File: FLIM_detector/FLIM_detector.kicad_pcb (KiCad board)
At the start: 2 copper layers, 19.8 x 18.4 mm, 17 parts, among them J1 Conn_01x02_Female, J2 Conn_01x02_Female, U1 OPA858xDSG, U2 LM4040DBZ-2.0, U3 AMS1117-5.0

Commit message: v0.7 power connector was flipped
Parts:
- moved J1 2.60 mm to (245.0, 18.3), turned to 90 degrees
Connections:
- D2 pad 2: Net-(J1-Pad2) -> Net-(D2-Pad2)
- J1 pad 1: GND -> Net-(D2-Pad2)
- J1 pad 2: Net-(J1-Pad2) -> GND
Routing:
- net Net-(J1-Pad2): track 3.37 -> 0.00 mm
- net Net-(D2-Pad2): track 0.00 -> 3.31 mm
- net +5V: track 21.4 -> 24.4 mm
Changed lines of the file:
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@@
   (net 7 "Net-(C3-Pad2)")
   (net 8 "Net-(J2-Pad1)")
-  (net 9 "Net-(J1-Pad2)")
+  (net 9 "Net-(D2-Pad2)")
   (footprint "Resistor_SMD:R_0402_1005Metric_Pad0.72x0.64mm_HandSolder" (layer "F.Cu")
     (at 248.4 27.6 90)
@@
       (net 7 "Net-(C3-Pad2)") (pinfunction "K") (pintype "passive"))
     (pad "2" smd rect (at 1.1 0 90) (size 0.5 0.5) (layers "F.Cu" "F.Paste" "F.Mask")
-      (net 9 "Net-(J1-Pad2)") (pinfunction "A") (pintype "passive"))
+      (net 9 "Net-(D2-Pad2)") (pinfunction "A") (pintype "passive"))
     (model "${KICAD6_3DMODEL_DIR}/Diode_SMD.3dshapes/D_SOD-323F.wrl"
       (offset (xyz 0 0 0))
@@
   )
   (footprint "Connector_PinHeader_2.54mm:PinHeader_1x02_P2.54mm_Vertical" (layer "F.Cu")
-    (at 247.6 18.325 -90)
+    (at 245 18.325 90)
     (descr "Through hole straight pin header, 1x02, 2.54mm pitch, single row")
     (tags "Through hole pin header THT 1x02 2.54mm single row")
@@
     (fp_line (start -1.27 3.81) (end -1.27 -0.635) (layer "F.Fab") (width 0.1))
     (fp_line (start -1.27 -0.635) (end -0.635 -1.27) (layer "F.Fab") (width 0.1))
-    (pad "1" thru_hole rect (at 0 0 270) (size 1.7 1.7) (drill 1) (layers *.Cu *.Mask)
-      (net 3 "GND") (pinfunction "Pin_1") (pintype "passive"))
-    (pad "2" thru_hole oval (at 0 2.54 270) (size 1.7 1.7) (drill 1) (layers *.Cu *.Mask)
-      (net 9 "Net-(J1-Pad2)") (pinfunction "Pin_2") (pintype "passive"))
+    (pad "1" thru_hole rect (at 0 0 90) (size 1.7 1.7) (drill 1) (layers *.Cu *.Mask)
+      (net 9 "Net-(D2-Pad2)") (pinfunction "Pin_1") (pintype "passive"))
+    (pad "2" thru_hole oval (at 0 2.54 90) (size 1.7 1.7) (drill 1) (layers *.Cu *.Mask)
+      (net 3 "GND") (pinfunction "Pin_2") (pintype "passive"))
     (model "${KICAD6_3DMODEL_DIR}/Connector_PinHeader_2.54mm.3dshapes/PinHeader_1x02_P2.54mm_Vertical.wrl"
       (offset (xyz 0 0 0))
@@
   (via (at 252.2 21.4) (size 0.8) (drill 0.4) (layers "F.Cu" "B.Cu") (free) (net 3))
   (segment (start 245.05 23) (end 251.35 23) (width 1) (layer "F.Cu") (net 4))
-  (segment (start 251.35 23.75) (end 252.3675 24.7675) (width 0.25) (layer "F.Cu") (net 4))
+  (segment (start 251.35 23.75) (end 252.3675 24.7675) (width 0.6) (layer "F.Cu") (net 4))
   (segment (start 254.949022 29.8) (end 251.7975 29.8) (width 0.4) (layer "F.Cu") (net 4))
   (segment (start 255.6 27.2) (end 255.6 29.149022) (width 0.4) (layer "F.Cu") (net 4))
   (segment (start 252.3675 26) (end 252.3675 27.1475) (width 0.4) (layer "F.Cu") (net 4))
+  (segment (start 251.2 21.2) (end 251.2 22.85) (width 0.6) (layer "F.Cu") (net 4))
   (segment (start 251.35 23) (end 251.35 23.75) (width 0.25) (layer "F.Cu") (net 4))
-  (segment (start 252.3675 24.7675) (end 252.3675 26) (width 0.25) (layer "F.Cu") (net 4))
+  (segment (start 252.3675 24.7675) (end 252.3675 26) (width 0.6) (layer "F.Cu") (net 4))
+  (segment (start 251.2 22.85) (end 251.35 23) (width 0.6) (layer "F.Cu") (net 4))
   (segment (start 252.6 26) (end 253.509511 26.909511) (width 0.4) (layer "F.Cu") (net 4))
   (segment (start 255.309511 26.909511) (end 255.6 27.2) (width 0.4) (layer "F.Cu") (net 4))
   (segment (start 255.6 29.149022) (end 255.374511 29.374511) (width 0.4) (layer "F.Cu") (net 4))
+  (segment (start 251.2 20.0625) (end 251.2 21.2) (width 0.6) (layer "F.Cu") (net 4))
   (segment (start 252.3675 26) (end 252.6 26) (width 0.4) (layer "F.Cu") (net 4))
   (segment (start 253.509511 26.909511) (end 255.309511 26.909511) (width 0.4) (layer "F.Cu") (net 4))
@@
   (segment (start 252.41 28.19) (end 254.19 28.19) (width 0.25) (layer "F.Cu") (net 8))
   (segment (start 242.6 19.8) (end 242.6 20.1) (width 0.25) (layer "F.Cu") (net 9))
-  (segment (start 243.2 19.2) (end 242.6 19.8) (width 0.5) (layer "F.Cu") (net 9))
-  (segment (start 244.185 19.2) (end 243.2 19.2) (width 0.5) (layer "F.Cu") (net 9))
-  (segment (start 245.06 18.325) (end 244.185 19.2) (width 0.5) (layer "F.Cu") (net 9))
+  (segment (start 242.6 19.8) (end 244.075 18.325) (width 0.5) (layer "F.Cu") (net 9))
+  (segment (start 244.075 18.325) (end 245 18.325) (width 0.5) (layer "F.Cu") (net 9))
   (zone (net 3) (net_name "GND") (layers F&B.Cu) (name "GND") (hatch edge 0.508)
     (connect_pads (clearance 0.508))

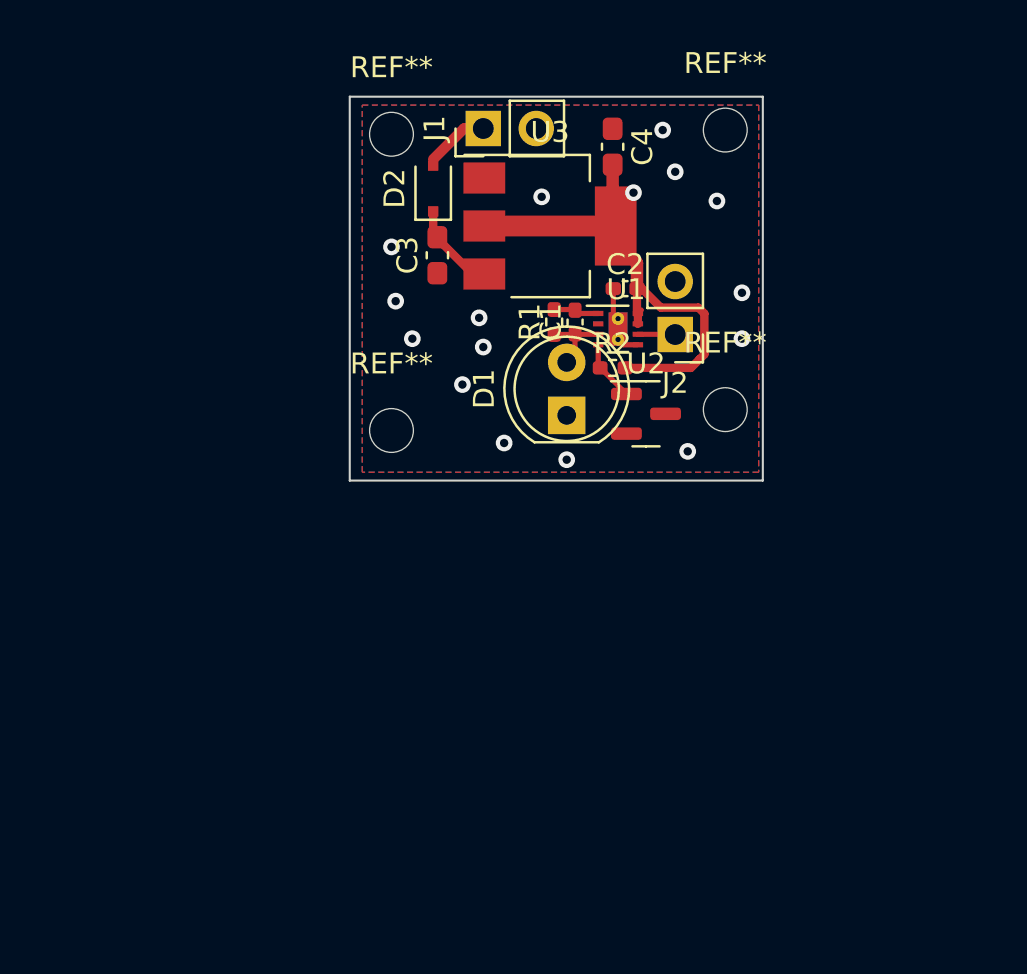
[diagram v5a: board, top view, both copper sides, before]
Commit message: v0.8 Routing was optimized
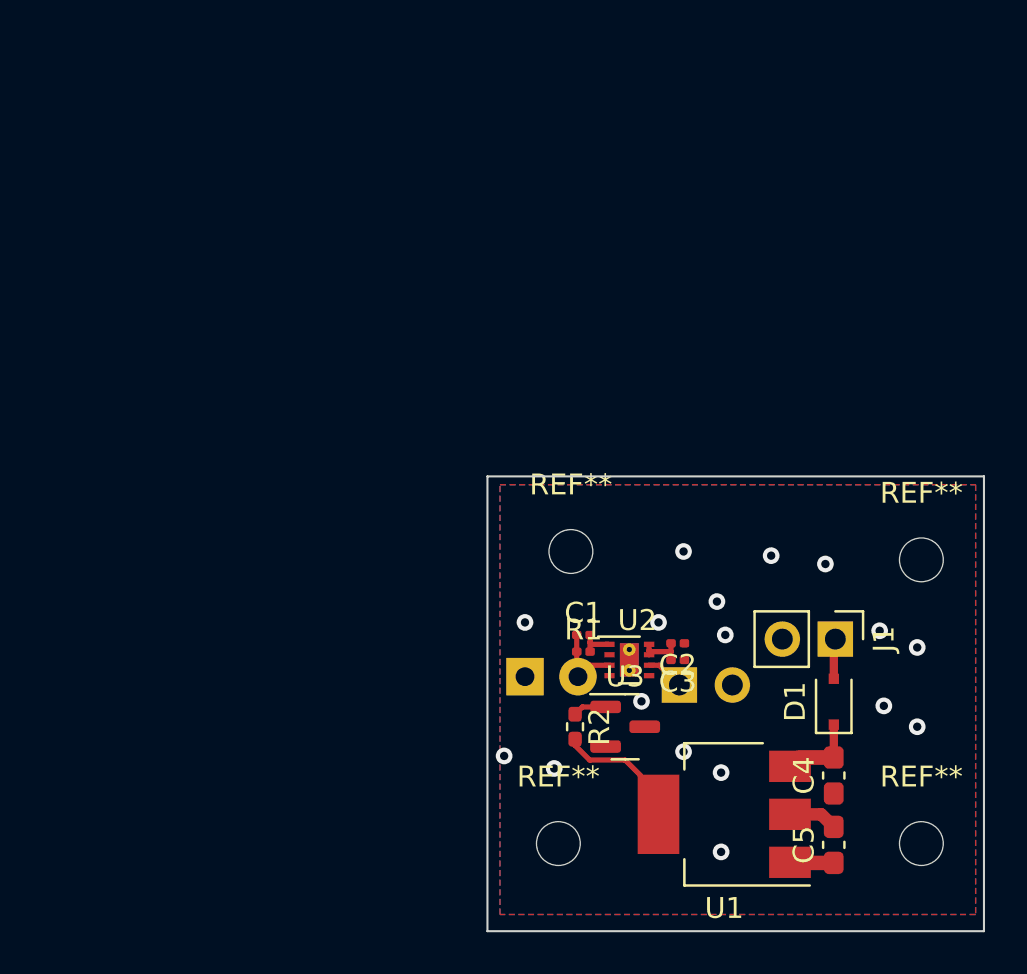
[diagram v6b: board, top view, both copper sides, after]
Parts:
- added C5: C, Capacitor_SMD:C_0603_1608Metric_Pad1.08x0.95mm_HandSolder, F.Cu at (261.8, 52.7)
- C1, C2: footprint Capacitor_SMD:C_0402_1005Metric_Pad0.74x0.62mm_HandSolder -> Capacitor_SMD:C_0201_0603Metric
- C3: footprint Capacitor_SMD:C_0603_1608Metric_Pad1.08x0.95mm_HandSolder -> Capacitor_SMD:C_0201_0603Metric
- D1: value LED -> PMEG4010CEJ; footprint LED_THT:LED_D5.0mm_Clear -> Diode_SMD:D_SOD-323F
- D2: value PMEG4010CEJ -> LED; footprint Diode_SMD:D_SOD-323F -> LED_THT:LED_D5.0mm_Clear; moved to B.Cu
- J2: moved to B.Cu
- R1: footprint Resistor_SMD:R_0402_1005Metric_Pad0.72x0.64mm_HandSolder -> Resistor_SMD:R_0201_0603Metric
- U1: value OPA858xDSG -> AMS1117-5.0; footprint Package_SON:WSON-8-1EP_2x2mm_P0.5mm_EP0.9x1.6mm_ThermalVias -> Package_TO_SOT_SMD:SOT-223-3_TabPin2
- U2: value LM4040DBZ-2.0 -> OPA858xDSG; footprint Package_TO_SOT_SMD:SOT-23 -> Package_SON:WSON-8-1EP_2x2mm_P0.5mm_EP0.9x1.6mm_ThermalVias
- U3: value AMS1117-5.0 -> LM4040DBZ-2.0; footprint Package_TO_SOT_SMD:SOT-223-3_TabPin2 -> Package_TO_SOT_SMD:SOT-23
- moved C4 31.9 mm to (261.8, 49.3), turned to 90 degrees
- moved J1 29.7 mm to (261.9, 42.8), turned to -90 degrees
- moved U3 24.3 mm to (251.8, 47.0)
- moved U1 23.8 mm to (256.6, 51.2), turned to 180 degrees
- moved D2 23.8 mm to (247.0, 44.6), turned to 0 degrees
- moved REF** 22.8 mm to (266.0, 52.6)
- moved REF** 22.6 mm to (266.0, 39.0)
- moved C3 22.6 mm to (254.3, 43.8), turned to 180 degrees
- moved REF** 21.8 mm to (249.2, 38.6)
- moved REF** 21.4 mm to (248.6, 52.6)
- moved D1 18.8 mm to (261.8, 45.8)
- moved R2 17.3 mm to (249.4, 47.0), turned to -90 degrees
- moved C2 17.2 mm to (254.3, 43.0), turned to 180 degrees
- moved J2 16.8 mm to (254.4, 45.0), turned to -90 degrees
- moved R1 15.9 mm to (249.8, 43.4), turned to 0 degrees
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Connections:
- C1 pad 1: Net-(C1-Pad1) -> Net-(U2-Pad3)
- C3 pad 2: Net-(C3-Pad2) -> +5V
- C4 pad 2: +5V -> Net-(C4-Pad2)
- D1 pad 1: GND -> Net-(C4-Pad2)
- D1 pad 2: Net-(C1-Pad1) -> Net-(D1-Pad2)
- D2 pad 1: Net-(C3-Pad2) -> GND
- D2 pad 2: Net-(D2-Pad2) -> Net-(U2-Pad3)
- J1 pad 1: Net-(D2-Pad2) -> Net-(D1-Pad2)
- R1 pad 1: Net-(C1-Pad1) -> Net-(U2-Pad3)
- U1 pad 1: Net-(C1-Pad2) -> GND
- U1 pad 2: unconnected-(U1-Pad2) -> +5V
- U1 pad 3: Net-(C1-Pad1) -> Net-(C4-Pad2)
- U2 pad 1: Net-(R2-Pad1) -> Net-(C1-Pad2)
- U2 pad 2: GND -> unconnected-(U2-Pad2)
- U2 pad 3: (no net) -> Net-(U2-Pad3)
- U3 pad 1: GND -> Net-(R2-Pad1)
- U3 pad 2: +5V -> GND
- U3 pad 3: Net-(C3-Pad2) -> (no net)
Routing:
- net +5V: track 24.4 -> 11.8 mm
- net Net-(C3-Pad2): track 4.67 -> 0.00 mm
- net Net-(C4-Pad2): track 0.00 -> 3.85 mm
- net Net-(U2-Pad3): track 0.00 -> 3.76 mm
- net Net-(C1-Pad1): track 3.70 -> 0.00 mm
- net Net-(D2-Pad2): track 3.31 -> 0.00 mm
- net Net-(D1-Pad2): track 0.00 -> 1.93 mm
- net Net-(R2-Pad1): track 2.93 -> 1.61 mm
- net (no net): vias 0 -> 1
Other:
- board size 19.8 x 18.4 mm -> 23.8 x 21.8 mm

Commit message: v0.9 subcompleted
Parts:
- moved REF** 1.28 mm to (248.2, 37.8)
- moved REF** 1.22 mm to (266.2, 37.8)
- moved REF** 1.08 mm to (248.2, 53.6)
- moved REF** 1.02 mm to (266.2, 53.6)
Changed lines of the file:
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@@
   )
   (footprint "MountingHole:MountingHole_2.1mm" (layer "F.Cu")
-    (at 249.2 38.6)
+    (at 248.2 37.8)
     (descr "Mounting Hole 2.1mm, no annular")
     (tags "mounting hole 2.1mm no annular")
@@
   )
   (footprint "MountingHole:MountingHole_2.1mm" (layer "F.Cu")
-    (at 266 52.6)
+    (at 266.2 53.6)
     (descr "Mounting Hole 2.1mm, no annular")
     (tags "mounting hole 2.1mm no annular")
@@
   )
   (footprint "MountingHole:MountingHole_2.1mm" (layer "F.Cu")
-    (at 248.6 52.6)
+    (at 248.2 53.6)
     (descr "Mounting Hole 2.1mm, no annular")
     (tags "mounting hole 2.1mm no annular")
@@
   )
   (footprint "MountingHole:MountingHole_2.1mm" (layer "F.Cu")
-    (at 266 39)
+    (at 266.2 37.8)
     (descr "Mounting Hole 2.1mm, no annular")
     (tags "mounting hole 2.1mm no annular")
@@
   (segment (start 250.8625 46.05) (end 249.7525 46.05) (width 0.25) (layer "F.Cu") (net 9))
   (zone (net 2) (net_name "GND") (layers F&B.Cu) (hatch edge 0.508)
-    (connect_pads (clearance 0.508))
-    (min_thickness 0.254) (filled_areas_thickness no)
-    (fill yes (thermal_gap 0.508) (thermal_bridge_width 0.508))
+    (connect_pads (clearance 0.2))
+    (min_thickness 0.2) (filled_areas_thickness no)
+    (fill yes (thermal_gap 0.2) (thermal_bridge_width 0.2))
     (polygon
       (pts

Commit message: v0.91 DRC was conducted
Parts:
- moved D2 0.34 mm to (246.7, 44.8)
- moved J2 0.20 mm to (254.4, 45.2)
- turned J1 to 90 degrees
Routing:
- net +5V: track 11.8 -> 35.8 mm
- net Net-(R2-Pad1): track 1.61 -> 3.19 mm
- net GND: vias 16 -> 19
- net (no net): vias 1 -> 0
